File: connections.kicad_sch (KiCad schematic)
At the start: 3 parts, among them J2 USB_B

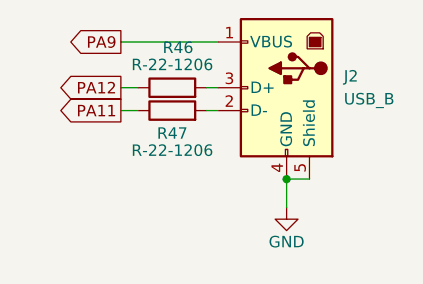
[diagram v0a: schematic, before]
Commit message: Working on the limiter
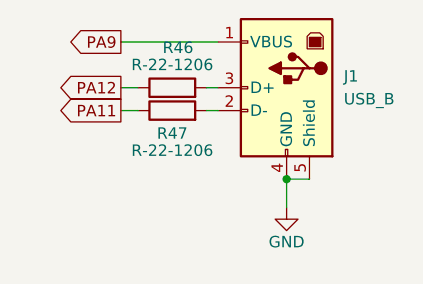
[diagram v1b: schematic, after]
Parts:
- renumbered J2 to J1
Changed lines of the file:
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@@
   (symbol (lib_id "power:GND") (at 44.45 41.91 0) (unit 1)
     (in_bom yes) (on_board yes)
-    (property "Reference" "#PWR084" (id 0) (at 44.45 48.26 0)
+    (property "Reference" "#PWR085" (id 0) (at 44.45 48.26 0)
       (effects (font (size 1.27 1.27)) hide)
     )
@@
   (symbol (lib_id "eurorack:USB_B") (at 44.45 28.575 0) (mirror y) (unit 1)
     (in_bom yes) (on_board yes) (fields_autoplaced)
-    (property "Reference" "J2" (id 0) (at 50.8 27.3049 0)
+    (property "Reference" "J1" (id 0) (at 50.8 27.3049 0)
       (effects (font (size 1.27 1.27)) (justify right))
     )

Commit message: working on AD inputs
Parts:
- renumbered R46 to R62, R47 to R63
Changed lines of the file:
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@@
   (symbol (lib_id "eurorack:R-22-1206") (at 31.75 31.115 90) (unit 1)
     (in_bom yes) (on_board yes)
-    (property "Reference" "R47" (id 0) (at 31.75 33.655 90))
+    (property "Reference" "R63" (id 0) (at 31.75 33.655 90))
     (property "Value" "R-22-1206" (id 1) (at 31.75 35.56 90))
     (property "Footprint" "Resistor_SMD:R_1206_3216Metric_Pad1.30x1.75mm_HandSolder" (id 2) (at 31.75 32.893 90)
@@
   (symbol (lib_id "power:GND") (at 44.45 41.91 0) (unit 1)
     (in_bom yes) (on_board yes)
-    (property "Reference" "#PWR085" (id 0) (at 44.45 48.26 0)
+    (property "Reference" "#PWR0125" (id 0) (at 44.45 48.26 0)
       (effects (font (size 1.27 1.27)) hide)
     )
@@
   (symbol (lib_id "eurorack:R-22-1206") (at 31.75 28.575 90) (unit 1)
     (in_bom yes) (on_board yes)
-    (property "Reference" "R46" (id 0) (at 32.385 24.13 90))
+    (property "Reference" "R62" (id 0) (at 32.385 24.13 90))
     (property "Value" "R-22-1206" (id 1) (at 31.75 26.035 90))
     (property "Footprint" "Resistor_SMD:R_1206_3216Metric_Pad1.30x1.75mm_HandSolder" (id 2) (at 31.75 30.353 90)

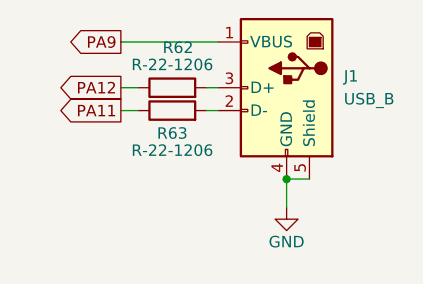
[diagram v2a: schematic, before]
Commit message: reannotated changed to LM324
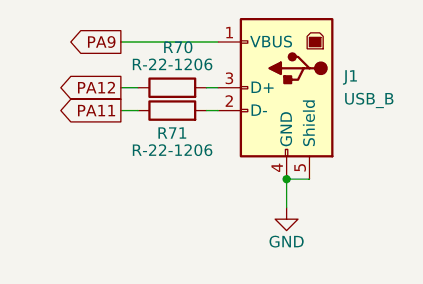
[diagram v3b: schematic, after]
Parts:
- renumbered R62 to R70, R63 to R71
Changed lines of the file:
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@@
   (symbol (lib_id "eurorack:R-22-1206") (at 31.75 31.115 90) (unit 1)
     (in_bom yes) (on_board yes)
-    (property "Reference" "R63" (id 0) (at 31.75 33.655 90))
+    (property "Reference" "R71" (id 0) (at 31.75 33.655 90))
     (property "Value" "R-22-1206" (id 1) (at 31.75 35.56 90))
     (property "Footprint" "Resistor_SMD:R_1206_3216Metric_Pad1.30x1.75mm_HandSolder" (id 2) (at 31.75 32.893 90)
@@
   (symbol (lib_id "power:GND") (at 44.45 41.91 0) (unit 1)
     (in_bom yes) (on_board yes)
-    (property "Reference" "#PWR0125" (id 0) (at 44.45 48.26 0)
+    (property "Reference" "#PWR0100" (id 0) (at 44.45 48.26 0)
       (effects (font (size 1.27 1.27)) hide)
     )
@@
   (symbol (lib_id "eurorack:R-22-1206") (at 31.75 28.575 90) (unit 1)
     (in_bom yes) (on_board yes)
-    (property "Reference" "R62" (id 0) (at 32.385 24.13 90))
+    (property "Reference" "R70" (id 0) (at 32.385 24.13 90))
     (property "Value" "R-22-1206" (id 1) (at 31.75 26.035 90))
     (property "Footprint" "Resistor_SMD:R_1206_3216Metric_Pad1.30x1.75mm_HandSolder" (id 2) (at 31.75 30.353 90)

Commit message: working on PCB, new iteratrion
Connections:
- net D-: now reaches J1.2 (D-), R71.2
- net D+: now reaches J1.3 (D+), R70.2
- net PA11 renamed USB_D-
- net PA12 renamed USB_D+
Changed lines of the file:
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@@
     (stroke (width 0) (type default) (color 0 0 0 0))
   )
-  (global_label "PA11" (shape output) (at 26.035 31.115 180) (fields_autoplaced)
+  (global_label "D+" (shape input) (at 36.195 28.575 90) (fields_autoplaced)
+    (effects (font (size 1.27 1.27)) (justify left))
+    (property "Intersheet References" "${INTERSHEET_REFS}" (id 0) (at 36.1156 23.3195 90)
+      (effects (font (size 1.27 1.27)) (justify left) hide)
+    )
+  )
+  (global_label "USB_D-" (shape output) (at 26.035 31.115 180) (fields_autoplaced)
     (effects (font (size 1.27 1.27)) (justify right))
-    (property "Intersheet References" "${INTERSHEET_REFS}" (id 0) (at 18.8443 31.0356 0)
+    (property "Intersheet References" "${INTERSHEET_REFS}" (id 0) (at 16.0019 31.0356 0)
       (effects (font (size 1.27 1.27)) (justify right) hide)
     )
@@
     )
   )
-  (global_label "PA12" (shape output) (at 26.035 28.575 180) (fields_autoplaced)
+  (global_label "USB_D+" (shape output) (at 26.035 28.575 180) (fields_autoplaced)
     (effects (font (size 1.27 1.27)) (justify right))
-    (property "Intersheet References" "${INTERSHEET_REFS}" (id 0) (at 18.8443 28.4956 0)
+    (property "Intersheet References" "${INTERSHEET_REFS}" (id 0) (at 16.0019 28.4956 0)
       (effects (font (size 1.27 1.27)) (justify right) hide)
     )
+  )
+  (global_label "D-" (shape input) (at 36.195 31.115 270) (fields_autoplaced)
+    (effects (font (size 1.27 1.27)) (justify right))
+    (property "Intersheet References" "${INTERSHEET_REFS}" (id 0) (at 36.1156 36.3705 90)
+      (effects (font (size 1.27 1.27)) (justify right) hide)
+    )

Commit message: wip v3
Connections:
- net GND renamed GND3
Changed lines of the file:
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@@
     (pin "2")
   )
-  (symbol (lib_id "power:GND") (at 44.45 41.91 0) (unit 1)
-    (in_bom yes) (on_board yes)
-    (property "Reference" "#PWR0100" (id 0) (at 44.45 48.26 0)
+  (symbol (lib_id "power:GND3") (at 44.45 41.91 0) (unit 1)
+    (in_bom yes) (on_board yes) (fields_autoplaced)
+    (property "Reference" "#PWR?" (id 0) (at 44.45 48.26 0)
       (effects (font (size 1.27 1.27)) hide)
     )
-    (property "Value" "GND" (id 1) (at 44.45 45.72 0))
+    (property "Value" "GND3" (id 1) (at 44.45 46.99 0))
     (property "Footprint" "" (id 2) (at 44.45 41.91 0)
       (effects (font (size 1.27 1.27)) hide)
